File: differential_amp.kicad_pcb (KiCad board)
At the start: 2 copper layers, 36.8 x 56.8 mm, 21 parts, among them J1 RJ45, P1 CON, P2 gnd_ref, U1 AD8422, U2 AD8609

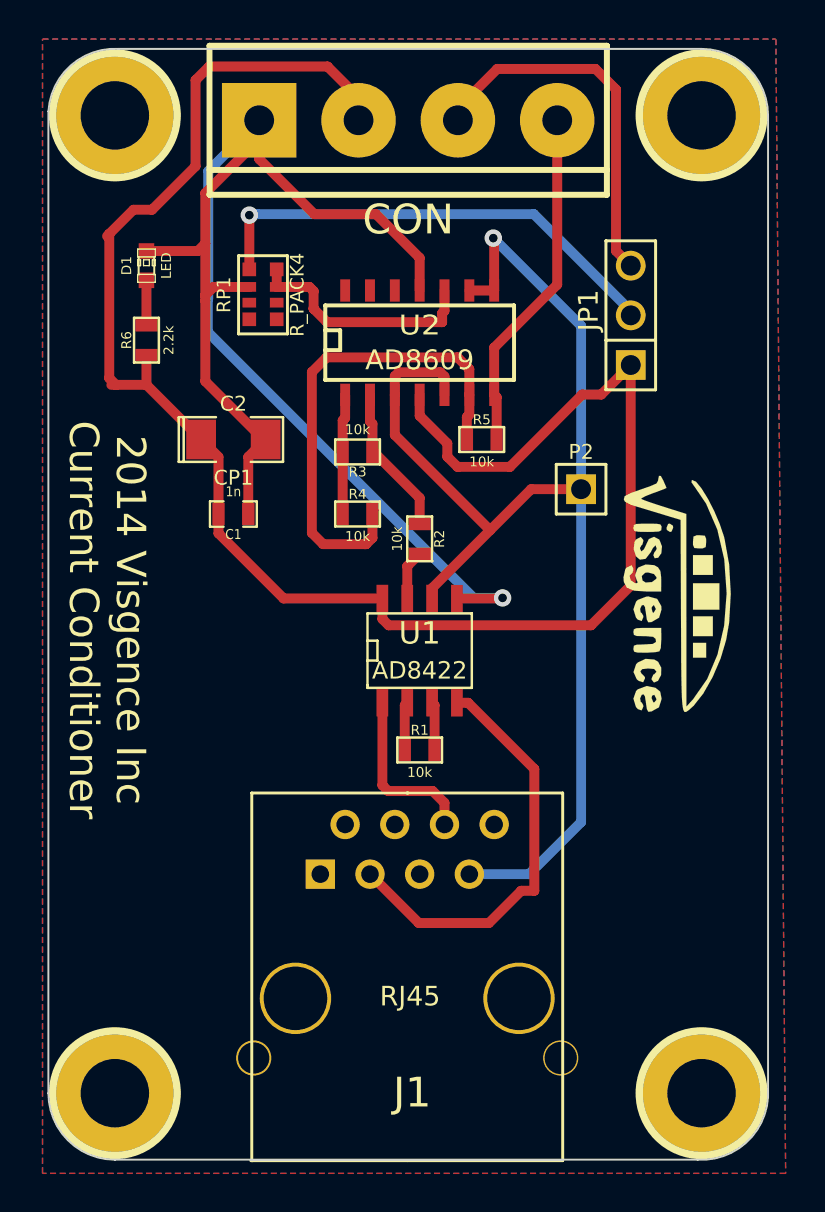
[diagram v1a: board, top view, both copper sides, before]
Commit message: Added gain selection and 5v output on rj45
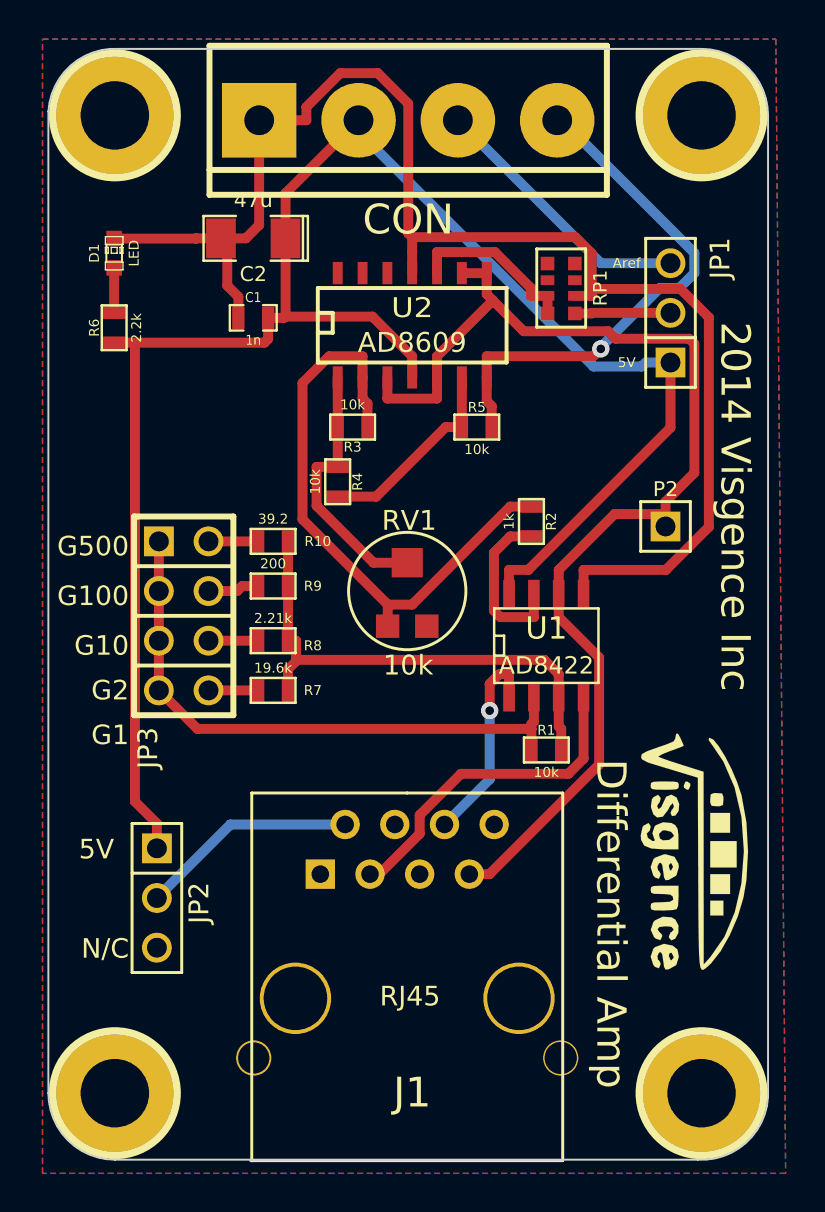
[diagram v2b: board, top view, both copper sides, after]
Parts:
- added G***: LOGO, LOGOMIRROR, B.Cu at (57.1, 58.7)
- added JP2: PWR, PIN_ARRAY_3X1, F.Cu at (44.3, 77.4)
- added JP3: GAIN_SEL, pin_array_4x2, F.Cu at (45.7, 63.0)
- added R10: 39.2, SM0603_VIS, F.Cu at (50.3, 59.2)
- added R7: 19.6k, SM0603_VIS, F.Cu at (50.3, 66.8)
- added R8: 2.21k, SM0603_VIS, F.Cu at (50.3, 64.3)
- added R9: 200, SM0603_VIS, F.Cu at (50.3, 61.5)
- added RV1: 10k, TC33X-2, F.Cu at (57.1, 61.7)
- C2: value CP1 -> 47u
- JP1: value JUMPER3 -> AREF
- R2: value 10k -> 1k
- moved RP1 15.3 mm to (65.0, 46.2), turned to 90 degrees
- moved G*** 13.2 mm to (71.9, 75.2)
- moved C2 10.3 mm to (49.3, 43.7), turned to 180 degrees
- moved C1 10.1 mm to (49.3, 47.8), turned to 0 degrees
- moved U1 6.48 mm to (64.3, 64.5)
- moved R1 6.48 mm to (64.3, 69.8)
- moved R2 5.78 mm to (63.5, 58.2)
- moved P2 4.72 mm to (70.4, 58.4)
- moved JP1 2.04 mm to (70.6, 47.5)
- moved R4 1.94 mm to (53.6, 56.1), turned to 270 degrees
- moved R6 1.77 mm to (42.2, 48.3)
- moved D1 1.77 mm to (42.2, 44.5)
- moved R3 1.30 mm to (54.4, 53.3)
- moved U2 0.97 mm to (57.4, 48.0)
- moved R5 0.68 mm to (60.7, 53.3)
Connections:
- J1 pad 2: (no net) -> N-0000017
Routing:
- net N-0000019: track 2.47 -> 30.2 mm
- net N-0000023: track 2.47 -> 25.9 mm
- net N-0000026: track 7.69 -> 31.0 mm
- net N-0000013: track 25.0 -> 4.90 mm, vias 1 -> 0
- net N-0000027: track 25.2 -> 10.4 mm
- net N-0000017: track 0.00 -> 11.2 mm
- net out: track 17.7 -> 27.0 mm, vias 0 -> 1
- net N-0000025: track 6.15 -> 13.5 mm
- net vgnd: track 66.3 -> 60.2 mm, vias 1 -> 0
- net N-0000015: track 2.55 -> 8.61 mm
- net AREF: track 19.3 -> 13.9 mm
- net N-0000031: track 21.7 -> 17.0 mm
- net GND: track 78.0 -> 74.2 mm, vias 1 -> 0
- net N-0000012: track 12.3 -> 8.80 mm
- net N-0000018: track 0.00 -> 2.65 mm
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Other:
- board text added: "5V"
- board text added: "Aref"
- board text added: "Differential Amp"
- board text added: "G1"
- board text added: "G10"
- board text added: "G100"
- board text added: "G2"
- board text added: "G500"
- board text added: "N/C"
- board text removed: "Current Conditioner"
